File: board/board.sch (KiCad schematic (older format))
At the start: 31 parts, among them J1 Conn_ARM_JTAG_SWD_10, J2 USB_B_Micro, J3 Conn_01x02, J4 Conn_01x08, J6 Conn_01x14, J7 Conn_Coaxial, J8 Wire Antenna, Q1 DMG2301L, SW1 SW_Push, U1 MCP1812A, U2 MCP73831-2-OT, U3 RFM95W-915S2

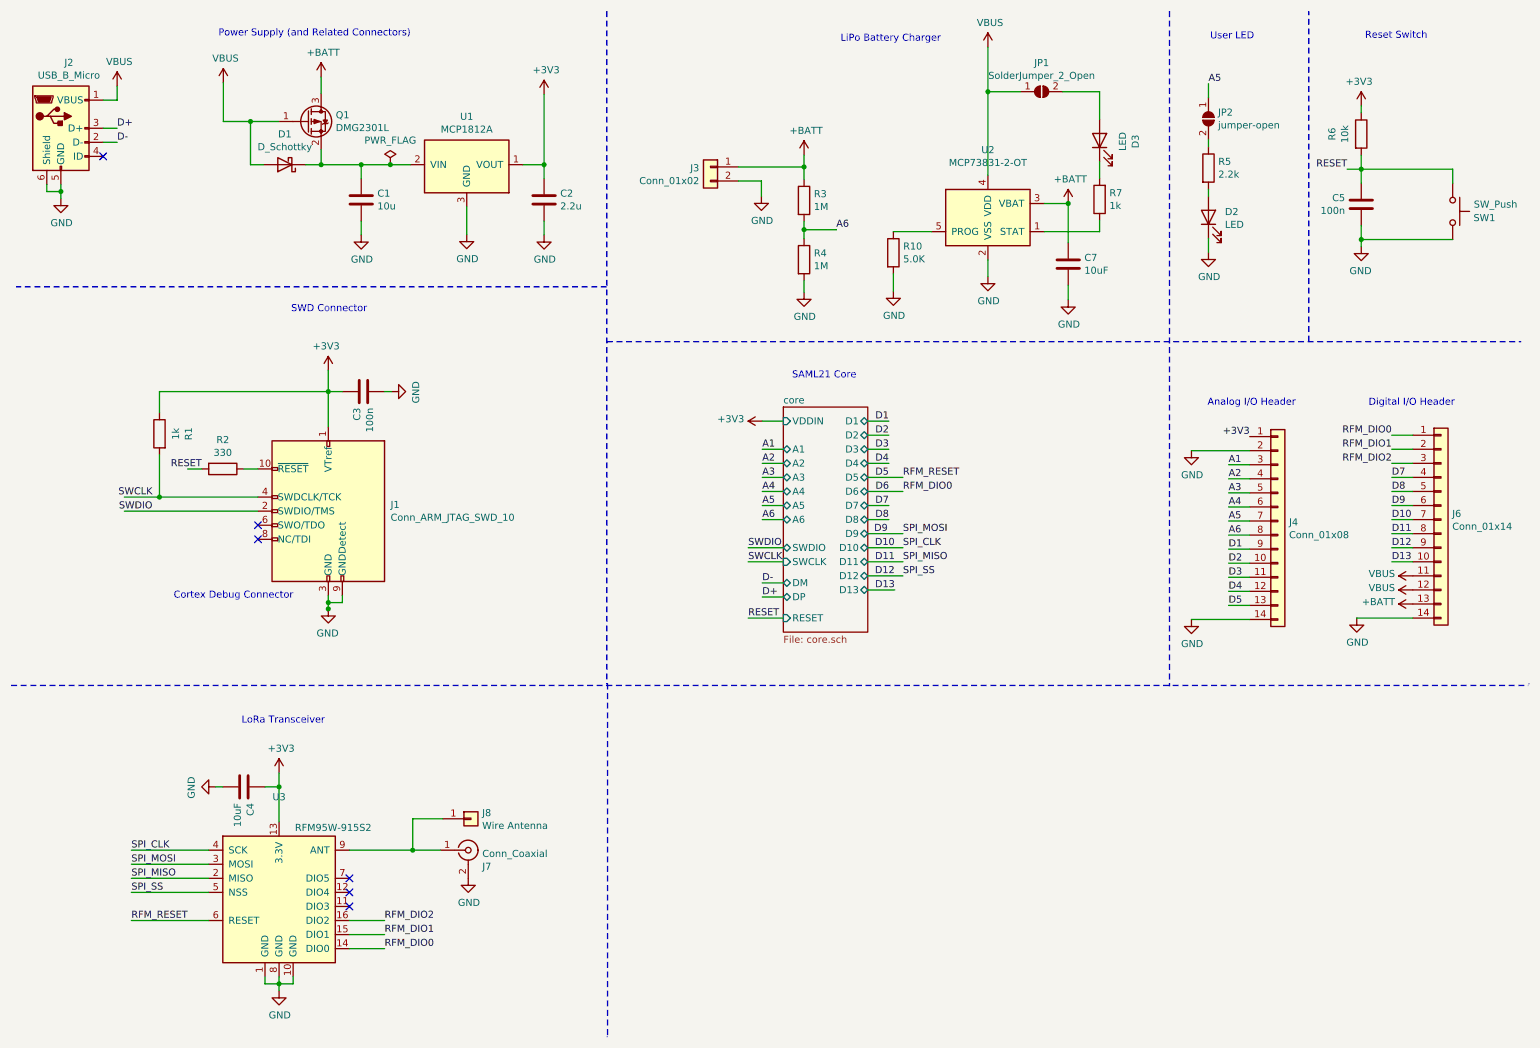
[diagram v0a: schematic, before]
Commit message: Changes to the board to prepare for RC1
- Added pull-down R (10k)
- Changed XTAL (ABS10)
- Changed values for load caps (C7-9) for XTAL
- Changed PROG value for batt controller (2k)
- Updated pin headers to include 3v3 and RFM_DIO1 pins
- Added jumpers to disable voltage divider (1M) on pin A6
- Repositioned USB connector, components and labels

Sign-off: LFRM, 03-23-2021
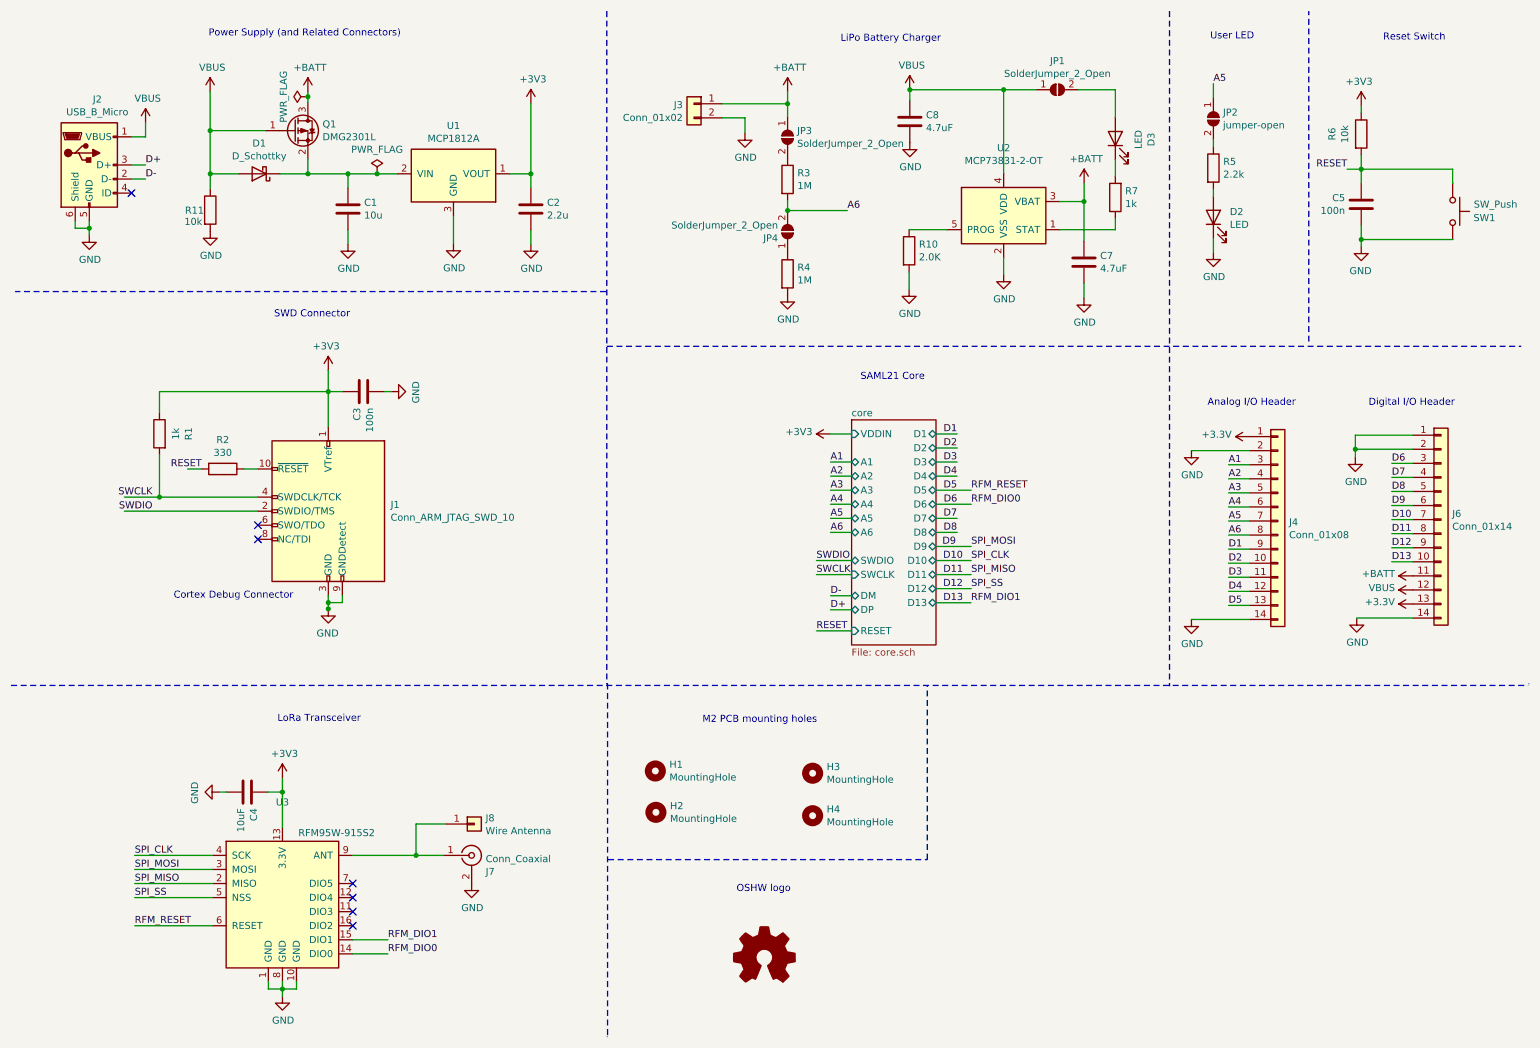
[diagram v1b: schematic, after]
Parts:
- added C8: 4.7uF, Capacitor_SMD:C_1206_3216Metric_Pad1.33x1.80mm_HandSolder, symbol Device:C
- added H1, H2, H3, H4: MountingHole, MountingHole:MountingHole_2.2mm_M2_Pad, symbol Mechanical:MountingHole
- added JP3, JP4: SolderJumper_2_Open, Jumper:SolderJumper-2_P1.3mm_Open_RoundedPad1.0x1.5mm, symbol Jumper:SolderJumper_2_Open
- added R11: 10k, Resistor_SMD:R_1206_3216Metric_Pad1.30x1.75mm_HandSolder, symbol Device:R
- C7: value 10uF -> 4.7uF
- R10: value 5.0K -> 2.0K
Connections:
- net labels added: +3.3V
- net labels removed: RFM_DIO2
- wire segments 154 -> 157
- no-connect marks 6 -> 7
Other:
- note added: "M2 PCB mounting holes"
- note added: "OSHW logo"
- moved on the sheet: C1, C2, C4, C7, D1, D2, D3, J2, J3, J7, J8, JP1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

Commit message: Pending fixes on rc1:
- added 10u cap for batt controller
- fixed poor connections on schematic, missed traces on D1 and C7
- changed RFMDIO1 pin to D1 (fixes issues w/ LoRa downlink)
- realigned components, repositioned traces
- increased pad sizes for hand-solderability on Q1 and U2
- overall retracing and re-alignment of components

Sign-off: LFRM, 07-03-2021
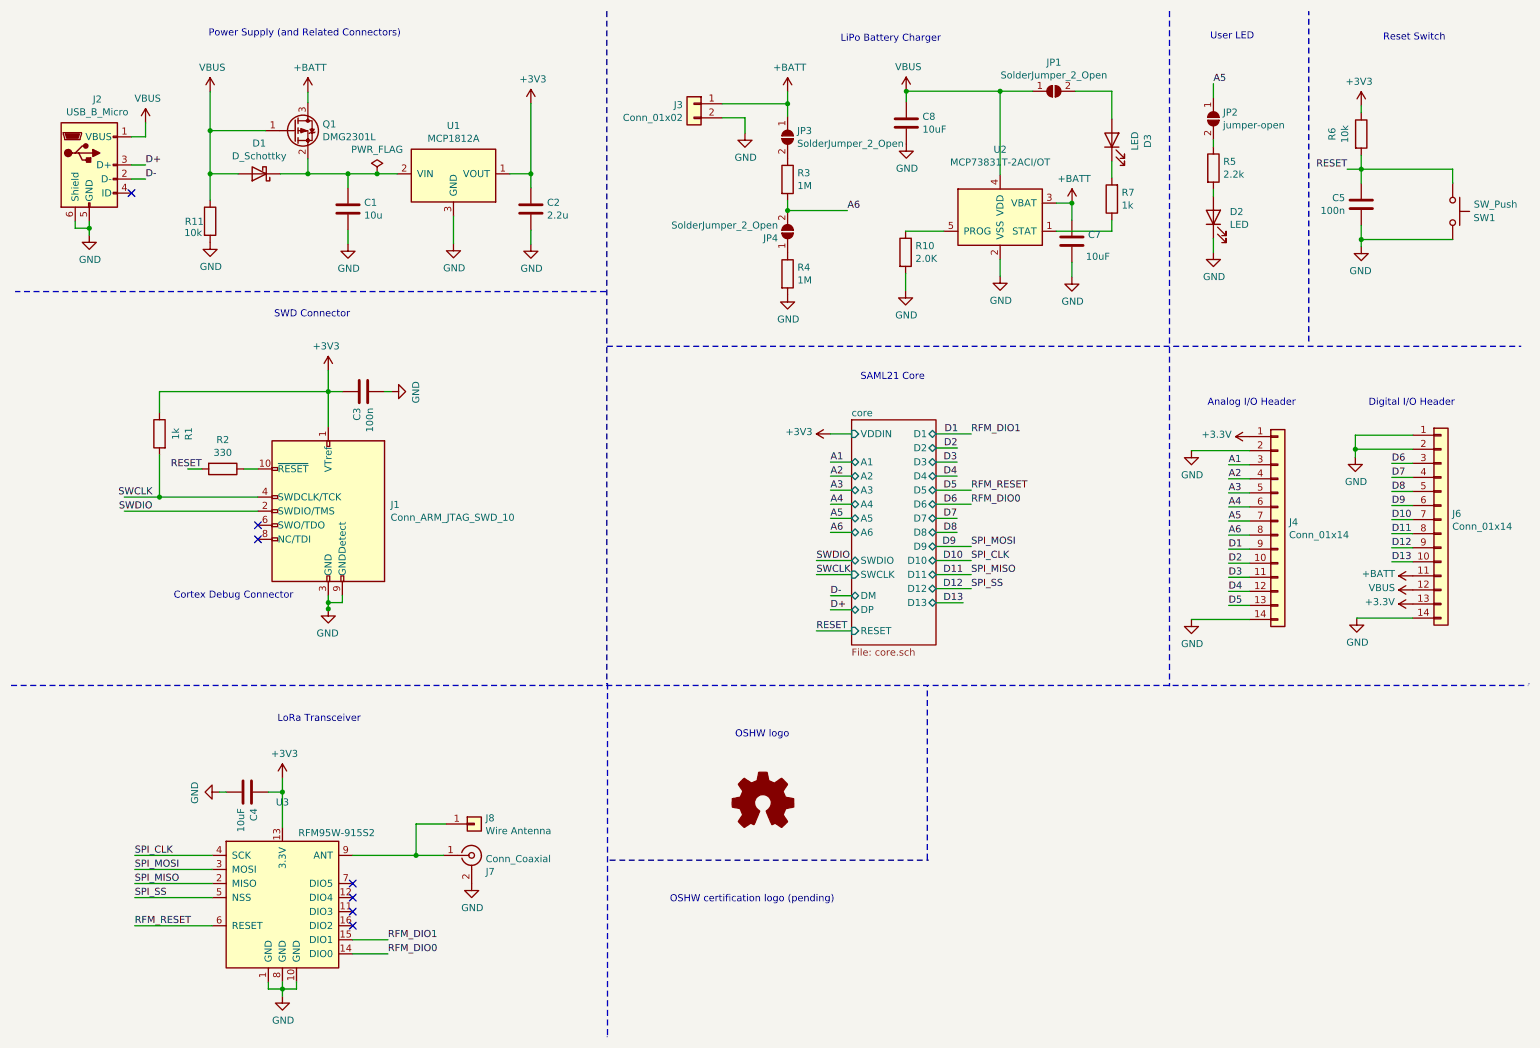
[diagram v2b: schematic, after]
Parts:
- removed H1, H2, H3, H4: MountingHole, MountingHole:MountingHole_2.2mm_M2_Pad, symbol Mechanical:MountingHole
- C7, C8: value 4.7uF -> 10uF
- J4: value Conn_01x08 -> Conn_01x14
- U2: value MCP73831-2-OT -> MCP73831T-2ACI/OT
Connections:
- wire segments 157 -> 152
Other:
- note added: "OSHW certification logo (pending)"
- note removed: "M2 PCB mounting holes"
- moved on the sheet: C7, C8, D3, JP1, R10, R11, R7, U2

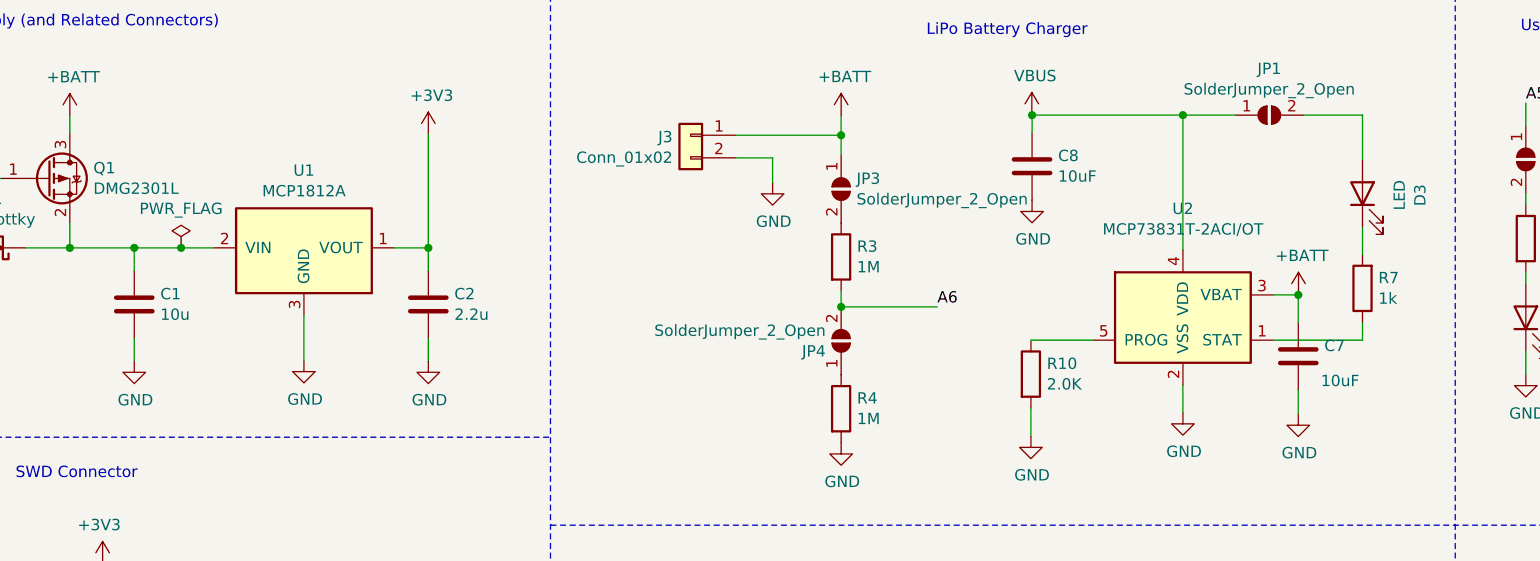
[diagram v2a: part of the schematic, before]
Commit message: fixed C1 value for LDO stabilization (2.2uF), adjusted current charge PROG (10K, 100mA), reverted values for C7 and C8 (4.7uF).
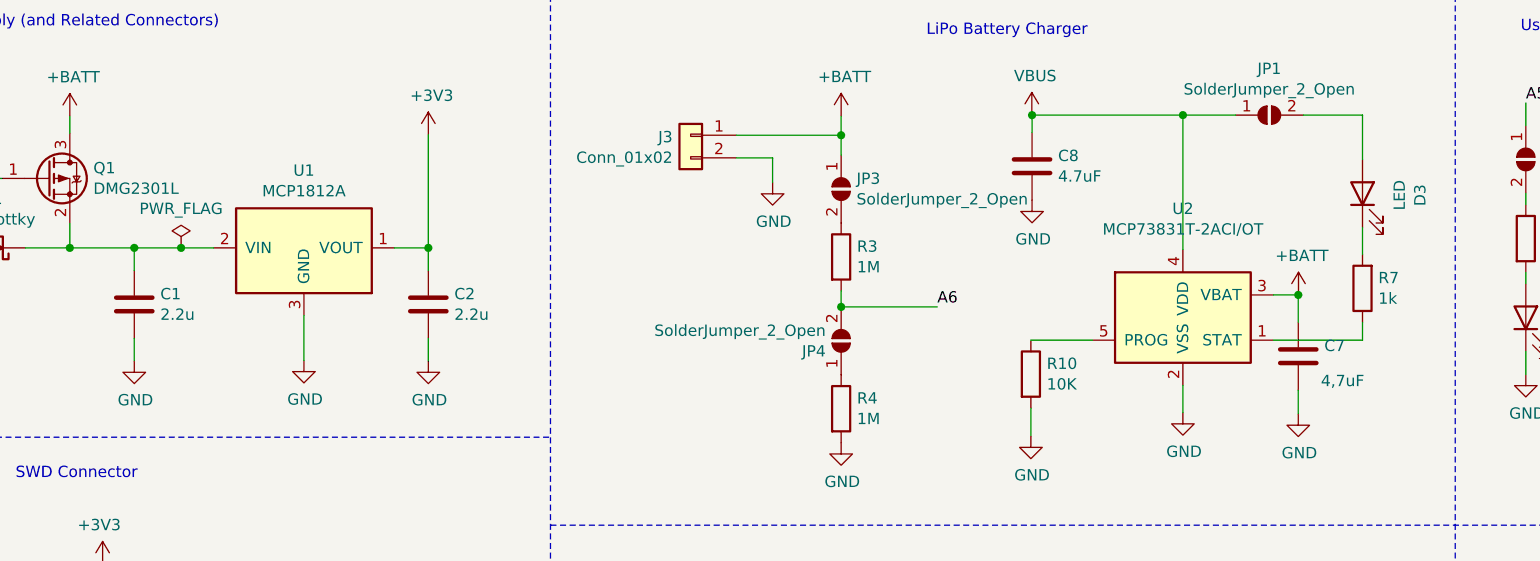
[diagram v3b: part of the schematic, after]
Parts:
- C1: value 10u -> 2.2u
- C7: value 10uF -> 4,7uF
- C8: value 10uF -> 4.7uF
- R10: value 2.0K -> 10K
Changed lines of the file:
@@
 P 2860 1907
 F 0 "C1" H 2975 1953 50  0000 L CNN
-F 1 "10u" H 2975 1862 50  0000 L CNN
+F 1 "2.2u" H 2975 1862 50  0000 L CNN
 F 2 "Capacitor_SMD:C_1206_3216Metric_Pad1.33x1.80mm_HandSolder" H 2898 1757 50  0001 C CNN
 F 3 "~" H 2860 1907 50  0001 C CNN
@@
 P 6824 2215
 F 0 "R10" H 6894 2261 50  0000 L CNN
-F 1 "2.0K" H 6894 2170 50  0000 L CNN
+F 1 "10K" H 6894 2170 50  0000 L CNN
 F 2 "Resistor_SMD:R_1206_3216Metric_Pad1.30x1.75mm_HandSolder" V 6754 2215 50  0001 C CNN
 F 3 "~" H 6824 2215 50  0001 C CNN
@@
 P 6829 1296
 F 0 "C8" H 6944 1342 50  0000 L CNN
-F 1 "10uF" H 6944 1251 50  0000 L CNN
+F 1 "4.7uF" H 6944 1251 50  0000 L CNN
 F 2 "Capacitor_SMD:C_1206_3216Metric_Pad1.33x1.80mm_HandSolder" H 6867 1146 50  0001 C CNN
 F 3 "~" H 6829 1296 50  0001 C CNN
@@
 P 8006 2136
 F 0 "C7" H 8121 2182 50  0000 L CNN
-F 1 "10uF" H 8106 2027 50  0000 L CNN
+F 1 "4,7uF" H 8106 2027 50  0000 L CNN
 F 2 "Capacitor_SMD:C_1206_3216Metric_Pad1.33x1.80mm_HandSolder" H 8044 1986 50  0001 C CNN
 F 3 "~" H 8006 2136 50  0001 C CNN
